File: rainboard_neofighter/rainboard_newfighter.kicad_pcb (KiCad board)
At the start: 2 copper layers, 260 x 253.6 mm, 95 parts, among them J1 Conn_01x02, J10 Conn_01x03, J11 SDS-50J, J12 SDS-50J, J13 Conn_01x02, J14 Conn_01x02, J15 Conn_01x02, J16 Conn_01x02, J17 Conn_01x02, J18 Conn_01x02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

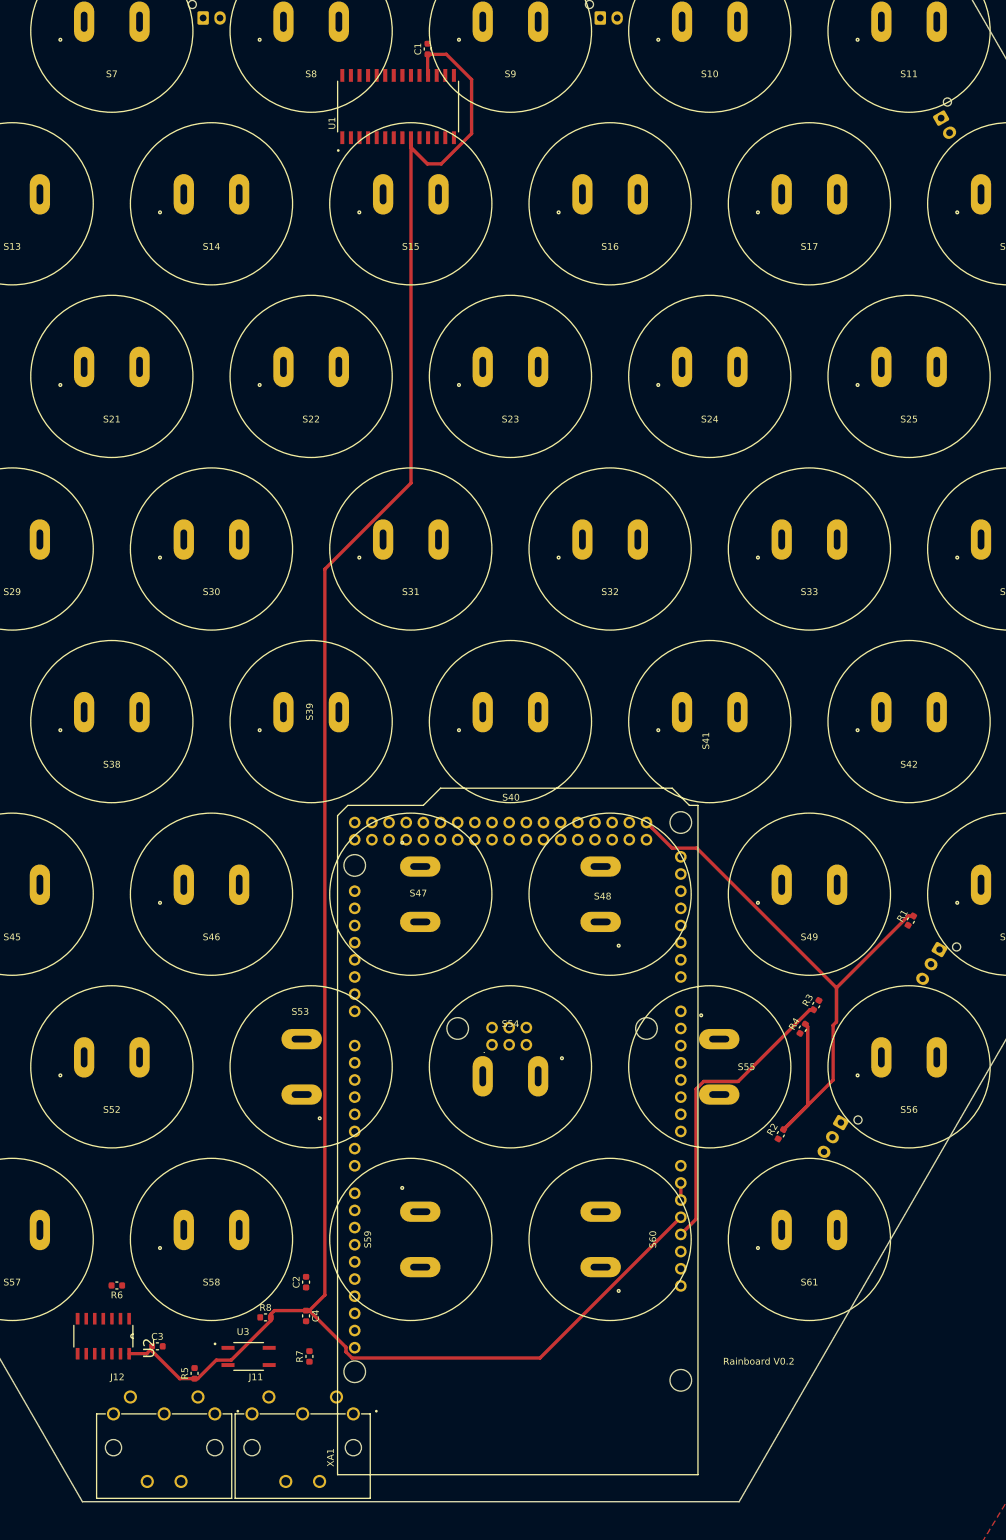
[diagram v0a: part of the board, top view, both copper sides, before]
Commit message: send MINI IN opto signal through schmitt trigger
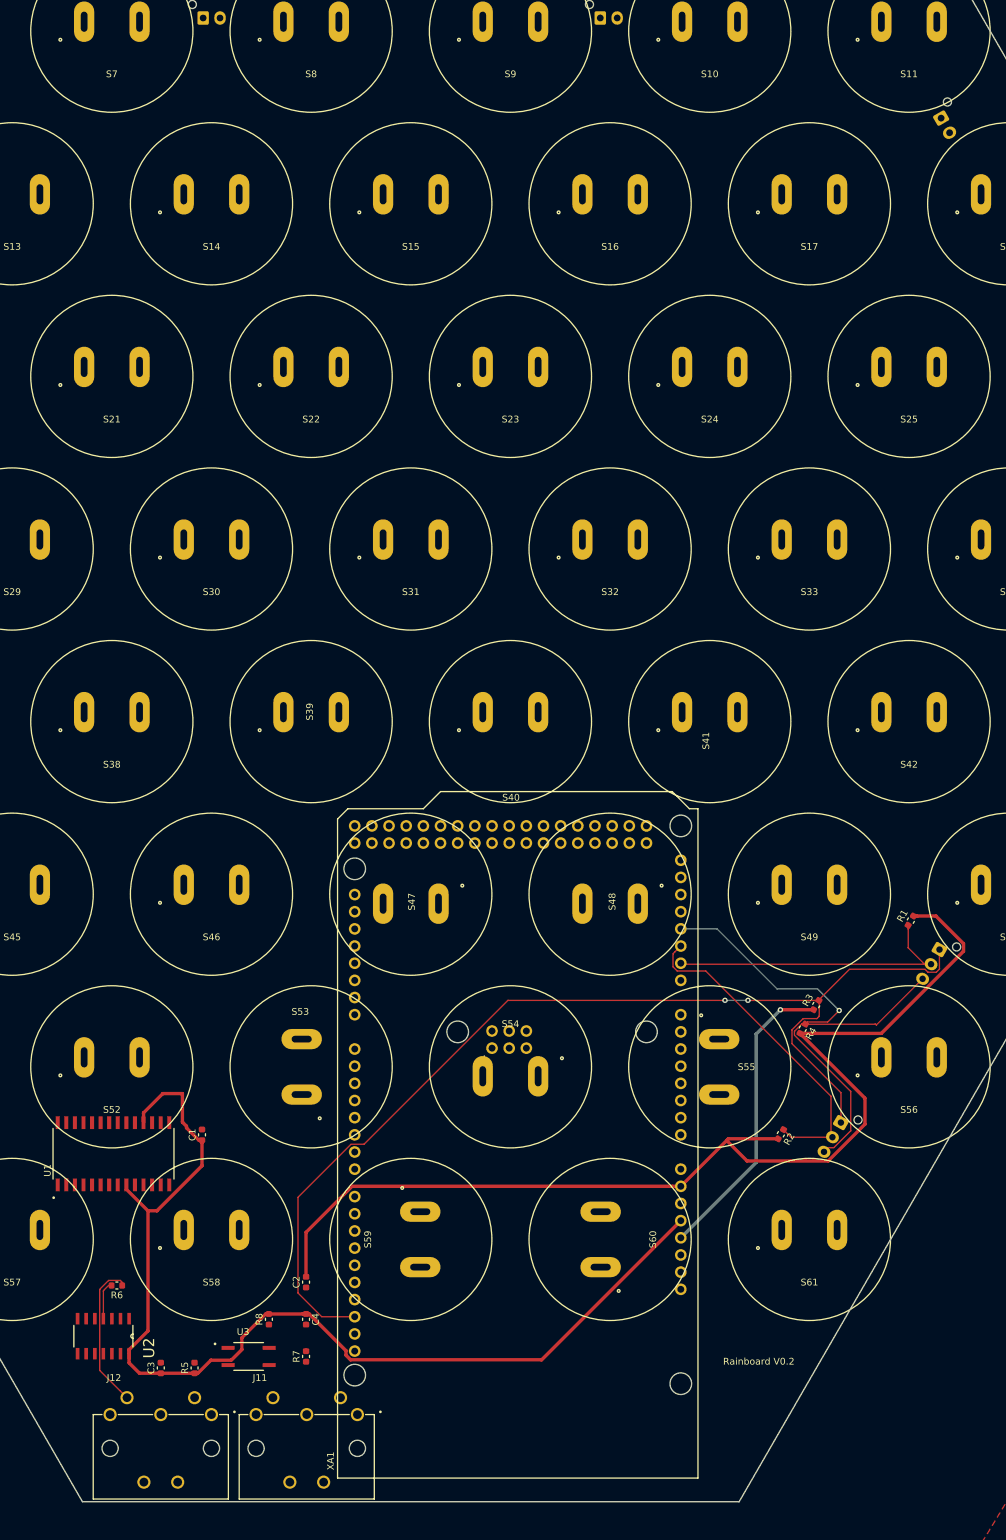
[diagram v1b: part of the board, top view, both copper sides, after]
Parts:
- moved C1 164.1 mm to (-30.9, 86.7)
- moved U1 160.6 mm to (-44.0, 89.5)
- moved C3 3.24 mm to (-37.0, 121.2), turned to 90 degrees
- moved R5 0.80 mm to (-32.0, 121.2)
- moved J11 0.61 mm to (-15.4, 128.1)
- moved R8 0.57 mm to (-21.0, 114.0), turned to 90 degrees
- moved J12 0.51 mm to (-37.0, 128.1)
- moved C4 0.50 mm to (-15.5, 114.0)
- moved R7 0.50 mm to (-15.5, 119.5)
- moved XA1 0.50 mm to (42.5, 137.5)
- turned R2 to 240 degrees
- turned R4 to 240 degrees
- turned S47 to 180 degrees
- turned S48 to 180 degrees
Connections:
- J12 pad 1: Net-(J12-Pad1) -> Earth
- J12 pad 3: Net-(J12-Pad3) -> Earth
- R8 pad 1: MIDI-IN -> Net-(R8-Pad1)
- U2 pad 11: Net-(U2-Pad11) -> Earth
- U2 pad 13: Net-(U2-Pad13) -> Earth
- U2 pad 5: Net-(U2-Pad5) -> Net-(R8-Pad1)
- U2 pad 8: Net-(U2-Pad8) -> MIDI-IN
- U2 pad 9: Net-(U2-Pad9) -> Net-(U2-Pad6)
- U3 pad 4: MIDI-IN -> Net-(R8-Pad1)
- XA1 pad GND3: Earth -> GNDA
- XA1 pad GND6: GNDA -> Earth
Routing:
- net AREF: track 0.00 -> 160.3 mm, vias 0 -> 2
- net 5V: track 312.6 -> 158.8 mm
- net BREF: track 0.00 -> 80.0 mm, vias 0 -> 1
- net GNDA: track 95.5 -> 163.0 mm
- net softpot-2: track 0.00 -> 48.7 mm
- net softpot-1: track 0.00 -> 44.8 mm
- net Net-(J12-Pad5): track 0.00 -> 22.2 mm
- net Net-(R6-Pad2): track 0.00 -> 5.67 mm
- net Earth: track 2.54 -> 0.00 mm
- net 3.3V: track 44.7 -> 44.8 mm, vias 0 -> 1

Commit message: fixed broken drill-hole
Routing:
- net AREF: track 160.3 -> 161.9 mm
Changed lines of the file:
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@@
     (thickness 1.6)
     (drawings 8)
-    (tracks 135)
+    (tracks 138)
     (zones 0)
     (modules 95)
@@
     (mod_text_size 1 1)
     (mod_text_width 0.15)
-    (pad_size 5.5 5.5)
-    (pad_drill 2.8)
+    (pad_size 3 6)
+    (pad_drill 1)
     (pad_to_mask_clearance 0.051)
     (solder_mask_min_width 0.25)
@@
     (add_net softpot-2)
   )
+  (module rainboard_newfighter:Sanwa-OBSF24-v2 (layer F.Cu)
+    (at 29.496825 51.09 180)
+    (fp_text reference S48 (at 0 6.35) (layer F.SilkS)
+      (effects (font (size 1 1) (thickness 0.15)))
+    )
+    (fp_text value SANWA-OBSF24 (at 0 -7.62) (layer F.Fab)
+      (effects (font (size 1 1) (thickness 0.15)))
+    )
+    (fp_circle (center -7.62 1.27) (end -7.42 1.27) (layer F.SilkS) (width 0.2))
+    (fp_circle (center 0 0) (end 12 0) (layer F.SilkS) (width 0.12))
+    (fp_circle (center 0 0) (end 12 0) (layer F.Fab) (width 0.12))
+    (pad 1 thru_hole oval (at -4.1 -1.4 180) (size 3 6) (drill oval 1 3) (layers *.Cu *.Mask)
+      (net 5 Earth))
+    (pad 2 thru_hole oval (at 4.1 -1.4 180) (size 3 6) (drill oval 1 3) (layers *.Cu *.Mask)
+      (net 44 button-48))
+  )
   (module Connector_JST:JST_XH_B3B-XH-AM_1x03_P2.50mm_Vertical (layer B.Cu)
     (at 63.6524 84.8868 240)
@@
   )
   (module rainboard_newfighter:Sanwa-OBSF24-v2 (layer F.Cu)
-    (at 29.496825 51.09 180)
-    (fp_text reference S48 (at -0.3196 -1.099625 270) (layer F.SilkS)
-      (effects (font (size 1 1) (thickness 0.15)))
-    )
-    (fp_text value SANWA-OBSF24 (at 0 -7.62) (layer F.Fab)
-      (effects (font (size 1 1) (thickness 0.15)))
-    )
-    (fp_circle (center -7.62 1.27) (end -7.42 1.27) (layer F.SilkS) (width 0.2))
-    (fp_circle (center 0 0) (end 12 0) (layer F.SilkS) (width 0.12))
-    (fp_circle (center 0 0) (end 12 0) (layer F.Fab) (width 0.12))
-    (pad 1 thru_hole oval (at -4.1 -1.4 180) (size 3 6) (drill oval 1 3) (layers *.Cu *.Mask)
-      (net 5 Earth))
-    (pad 2 thru_hole oval (at 4.1 -1.4 180) (size 3 6) (drill oval 1 3) (layers *.Cu *.Mask)
-      (net 44 button-48))
-  )
-  (module rainboard_newfighter:Sanwa-OBSF24-v2 (layer F.Cu)
     (at 29.496825 102.18 90)
     (fp_text reference S60 (at 0 6.35 90) (layer F.SilkS)
@@
   (segment (start -13.176 113.624) (end -8.3 113.624) (width 0.20066) (layer F.Cu) (net 108))
   (segment (start -16.7 110.1) (end -13.176 113.624) (width 0.20066) (layer F.Cu) (net 108))
+  (segment (start -16.7 110.0125) (end -16.7 110.1) (width 0.20066) (layer F.Cu) (net 108))
+  (segment (start -15.975 109.2875) (end -16.7 110.0125) (width 0.20066) (layer F.Cu) (net 108))
+  (segment (start -15.5 109.2875) (end -15.975 109.2875) (width 0.20066) (layer F.Cu) (net 108))
   (segment (start 57.853218 70.318005) (end 58.39375 70.318005) (width 0.20066) (layer F.Cu) (net 115))
   (segment (start 57.83808 70.318005) (end 57.853218 70.318005) (width 0.20066) (layer F.Cu) (net 115))
